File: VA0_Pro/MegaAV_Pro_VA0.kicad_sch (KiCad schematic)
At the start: 179 parts, among them CN1 MD-90SM_MD2, P1 SMD_Conn_01x01, U1 CD4070, U2 74HCT123, U3 TS924, U4 THS7374, U5 ICS501, U6 TS922, U7 TS924, U8 AD723, U9 NCV8114ASN250T1G

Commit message: MegaAV VA0 CE PCBA updates
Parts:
- U6: footprint Package_SO:TSSOP-8_4.4x3mm_P0.65mm -> Package_SO:SO-8_3.9x4.9mm_P1.27mm
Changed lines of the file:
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@@
 			)
 		)
-		(property "Footprint" "Package_SO:TSSOP-8_4.4x3mm_P0.65mm"
+		(property "Footprint" "Package_SO:SO-8_3.9x4.9mm_P1.27mm"
 			(at 320.04 133.35 0)
 			(effects
@@
 			)
 		)
-		(property "Footprint" "Package_SO:TSSOP-8_4.4x3mm_P0.65mm"
+		(property "Footprint" "Package_SO:SO-8_3.9x4.9mm_P1.27mm"
 			(at 226.8678 242.2728 0)
 			(effects
@@
 			)
 		)
-		(property "Footprint" "Package_SO:TSSOP-8_4.4x3mm_P0.65mm"
+		(property "Footprint" "Package_SO:SO-8_3.9x4.9mm_P1.27mm"
 			(at 320.04 105.41 0)
 			(effects

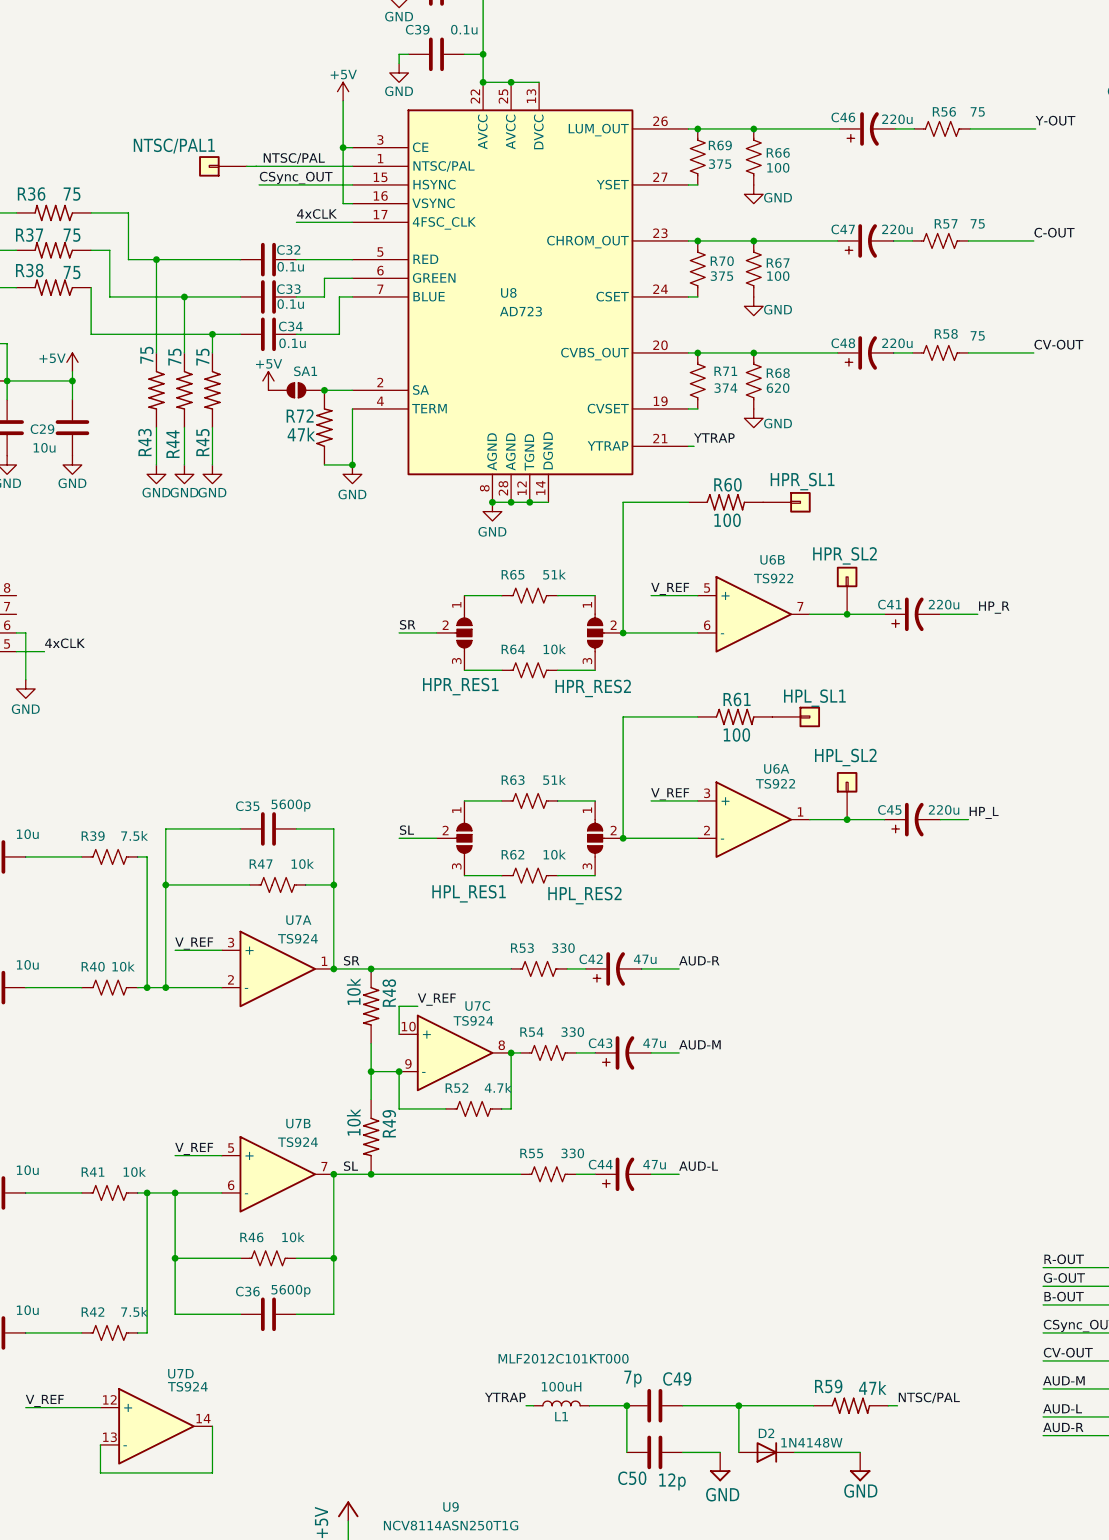
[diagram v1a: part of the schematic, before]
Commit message: Fixed VA0 errors
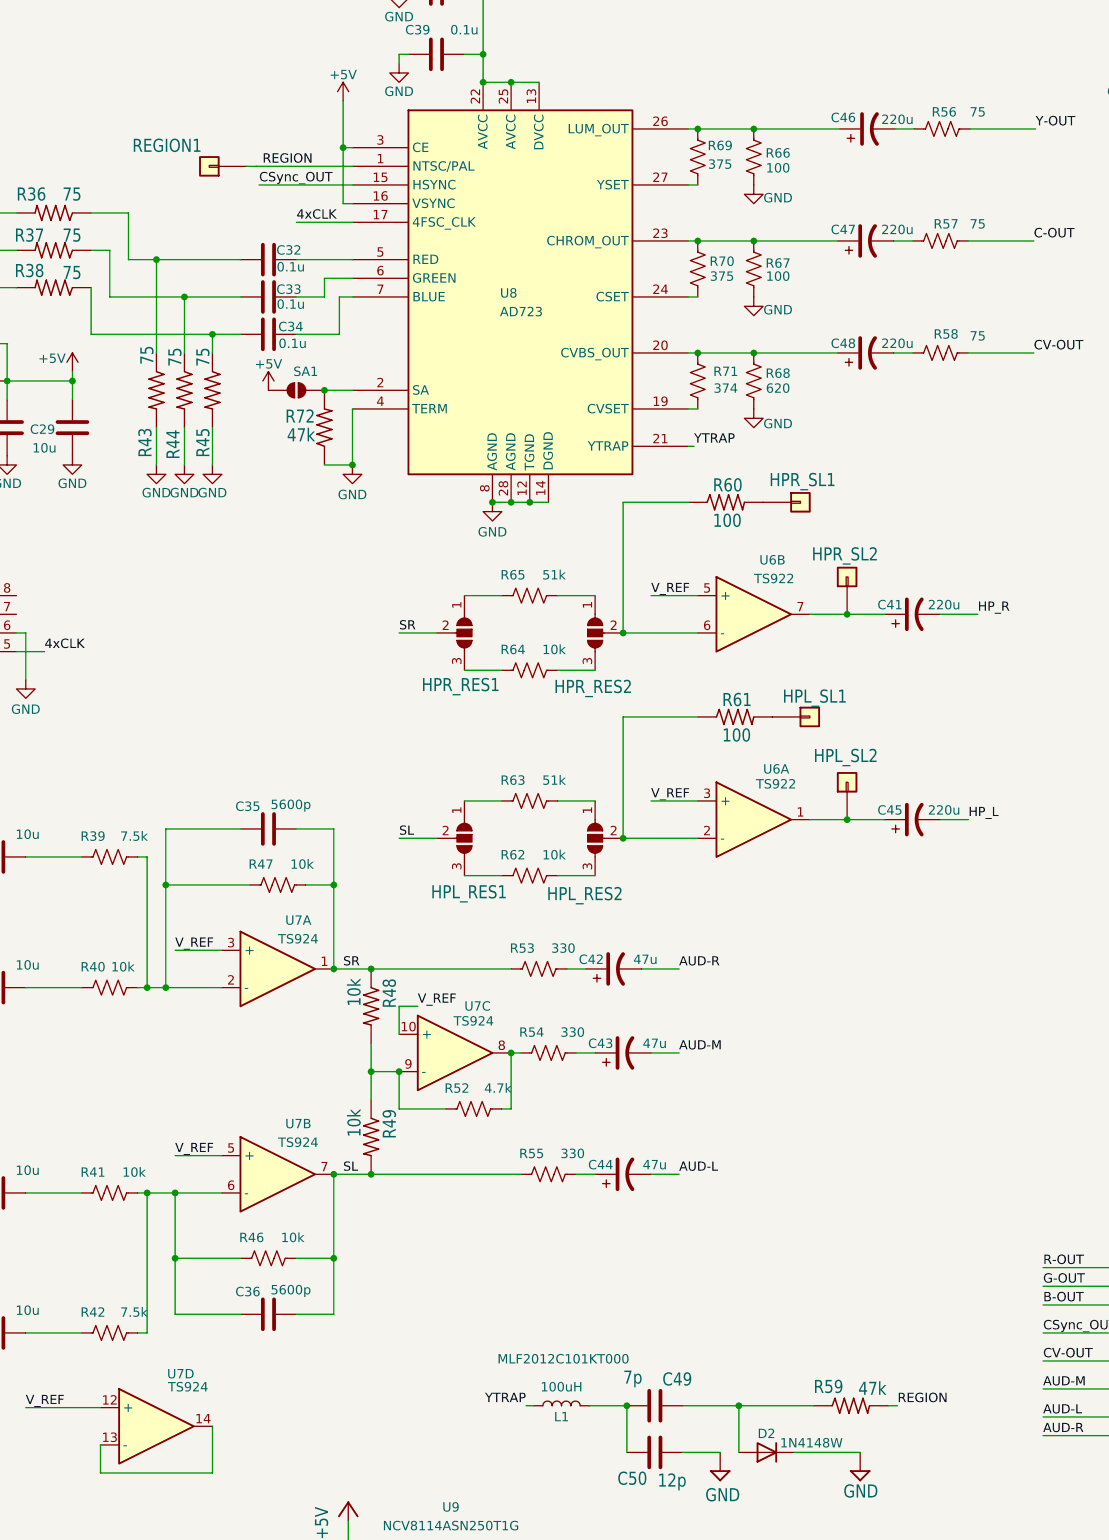
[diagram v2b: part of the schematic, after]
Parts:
- C28: footprint Capacitor_SMD:C_0402_1005Metric -> Capacitor_SMD:C_0805_2012Metric
- D1, D2: footprint Diode_SMD:D_SOD-882 -> Diode_SMD:D_SOD-323F
- renumbered NTSC/PAL1 to REGION1
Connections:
- net NTSC/PAL renamed REGION
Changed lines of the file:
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@@
 		)
 	)
-	(label "NTSC{slash}PAL"
+	(label "REGION"
 		(at 339.598 213.106 0)
 		(effects
@@
 		)
 	)
-	(label "NTSC{slash}PAL"
+	(label "REGION"
 		(at 253.1837 44.45 0)
 		(effects
@@
 			)
 		)
-		(property "Footprint" "Capacitor_SMD:C_0402_1005Metric"
+		(property "Footprint" "Capacitor_SMD:C_0805_2012Metric"
 			(at 219.4052 83.82 0)
 			(effects
@@
 			)
 		)
-		(property "Footprint" "Diode_SMD:D_SOD-882"
+		(property "Footprint" "Diode_SMD:D_SOD-323F"
 			(at 78.74 120.015 0)
 			(effects
@@
 			)
 		)
-		(property "Footprint" "Diode_SMD:D_SOD-882"
+		(property "Footprint" "Diode_SMD:D_SOD-323F"
 			(at 321.818 215.011 0)
 			(effects
@@
 		(on_board yes)
 		(dnp no)
-		(property "Reference" "NTSC/PAL1"
+		(property "Reference" "REGION1"
 			(at 235.4705 42.6996 0)
 			(effects
@@
 			(project "MegaAV_VA1"
 				(path "/672e6c7a-d310-45d1-a117-69a32c775d0f"
-					(reference "NTSC/PAL1")
+					(reference "REGION1")
 					(unit 1)
 				)
